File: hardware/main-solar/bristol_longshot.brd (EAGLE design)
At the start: 14 x 64 mm, 84 parts, among them U1 SAM_D20E, U10 TPS62243, U11 TPS3808, U12 74LVC1G04GW, U13 SPV1040, U14 LT4054ES5-4.2, U2 SI4060, U3 UBLOX_MAX, U4 TPS62243, U5 TG-5006CJ, U6 TG-5006CJ, U7 TPS3123, U8 SN74LVC1G32DCKR, U9 SE880, Y1 ABS05

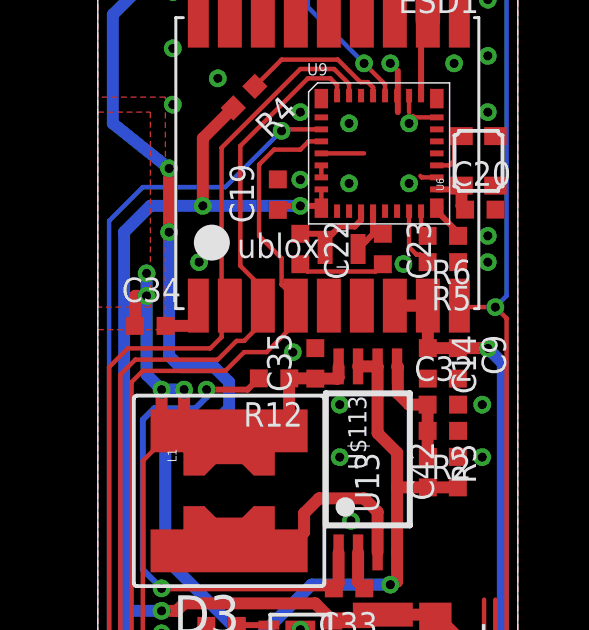
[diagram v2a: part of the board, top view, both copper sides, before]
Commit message: Added 0603 cap to vsolar
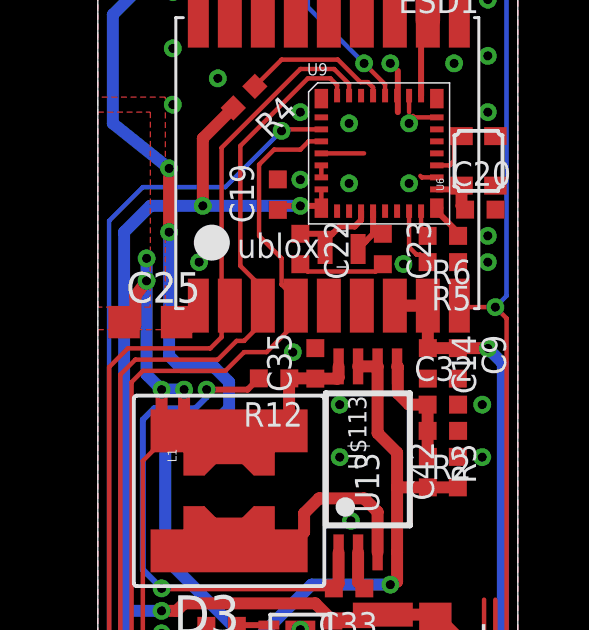
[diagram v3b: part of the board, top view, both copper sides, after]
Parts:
- removed C34: 4.7µF, microbuilder_v3:_0402
- added C25: 10µF, resistor:C0603K
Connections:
- net GND: now also C25.2; no longer C34.2
- net VSOLAR: now also C25.1; no longer C34.1
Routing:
- net GND: track 40.6 -> 39.6 mm
- net VSOLAR: track 52.6 -> 53.3 mm
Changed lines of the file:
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@@
 <element name="C33" library="microbuilder_v3" package="_0402" value="1nF" x="8.375" y="38.625" rot="R180"/>
 <element name="R12" library="microbuilder_v3" package="_0402" value="1kΩ" x="5.875" y="45.625" rot="R180"/>
-<element name="C34" library="microbuilder_v3" package="_0402" value="4.7µF" x="1.75" y="47.375"/>
 <element name="C35" library="microbuilder_v3" package="_0402" value="4.7µF" x="7.25" y="46.125" rot="R90"/>
 <element name="C36" library="microbuilder_v3" package="_0402" value="4.7µF" x="7" y="26.875"/>
@@
 <element name="R21" library="microbuilder_v3" package="_0402" value="DNP" x="5" y="26.875"/>
 <element name="L1" library="PecanFemto4" package="LPS3015" value="10uH LPS3015" x="4.375" y="41.875" rot="R270"/>
+<element name="C25" library="resistor" package="C0603K" value="10µF" x="1.75" y="47.5"/>
 </elements>
 <signals>
@@
 <contactref element="C31" pad="2"/>
 <contactref element="C33" pad="1"/>
-<contactref element="C34" pad="2"/>
 <contactref element="C35" pad="2"/>
 <contactref element="C36" pad="2"/>
@@
 <via x="7.5" y="25.125" extent="1-16" drill="0.3"/>
 <via x="12.8125" y="44.75" extent="1-16" drill="0.3"/>
-<wire x1="2.258" y1="47.375" x2="3.25" y2="47.375" width="0.4" layer="1"/>
 <via x="12.8125" y="43" extent="1-16" drill="0.3"/>
 <via x="8.0625" y="44.75" extent="1-16" drill="0.3"/>
@@
 <wire x1="1.5" y1="18.125" x2="1.383" y2="18.242" width="0.4" layer="1"/>
 <wire x1="1.383" y1="18.242" x2="1.375" y2="18.242" width="0.4" layer="1"/>
+<contactref element="C25" pad="2"/>
 </signal>
 <signal name="SWDIO">
@@
 <contactref element="U13" pad="8"/>
 <contactref element="C35" pad="1"/>
-<contactref element="C34" pad="1"/>
 <contactref element="U$113" pad="P$1"/>
 <wire x1="7.25" y1="45.617" x2="7.242" y2="45.625" width="0.4" layer="1"/>
@@
 <wire x1="6.25" y1="22.125" x2="1.75" y2="22.125" width="0.15" layer="1"/>
 <wire x1="1.75" y1="22.125" x2="1.5" y2="22.375" width="0.15" layer="1"/>
-<via x="1.625" y="49.125" extent="1-16" drill="0.3"/>
-<via x="1.625" y="48.375" extent="1-16" drill="0.3"/>
+<via x="1.625" y="49.625" extent="1-16" drill="0.3"/>
+<via x="1.625" y="48.875" extent="1-16" drill="0.3"/>
 <via x="2.125" y="45.25" extent="1-16" drill="0.3"/>
 <via x="2.875" y="45.25" extent="1-16" drill="0.3"/>
-<wire x1="1.625" y1="49.125" x2="1.625" y2="48.375" width="0.4" layer="16"/>
-<wire x1="1.625" y1="48.375" x2="1.625" y2="45.75" width="0.4" layer="16"/>
+<wire x1="1.625" y1="49.625" x2="1.625" y2="48.875" width="0.4" layer="16"/>
+<wire x1="1.625" y1="48.875" x2="1.625" y2="45.75" width="0.4" layer="16"/>
 <wire x1="1.625" y1="45.75" x2="2.125" y2="45.25" width="0.4" layer="16"/>
 <wire x1="2.125" y1="45.25" x2="2.875" y2="45.25" width="0.4" layer="16"/>
 <wire x1="2.125" y1="45.25" x2="2.125" y2="43.375" width="0.4" layer="1"/>
 <wire x1="2.875" y1="45.25" x2="2.875" y2="43.625" width="0.4" layer="1"/>
-<wire x1="1.242" y1="47.375" x2="1.25" y2="47.383" width="0.4" layer="1"/>
 <wire x1="1.25" y1="47.383" x2="1.25" y2="48.375" width="0.4" layer="1"/>
-<wire x1="1.25" y1="48.375" x2="1.625" y2="48.375" width="0.4" layer="1"/>
+<wire x1="1.25" y1="48.375" x2="1.625" y2="48.875" width="0.4" layer="1"/>
 <polygon width="0.2" layer="1">
 <vertex x="0" y="54.5"/>
@@
 <wire x1="3.32725" y1="42.5735" x2="3.361540625" y2="42.5735" width="0.2" layer="1"/>
 <wire x1="3.361540625" y1="42.5735" x2="3.552040625" y2="42.764" width="0.2" layer="1"/>
+<contactref element="C25" pad="1"/>
 </signal>
 <signal name="VBATT_SENSE">

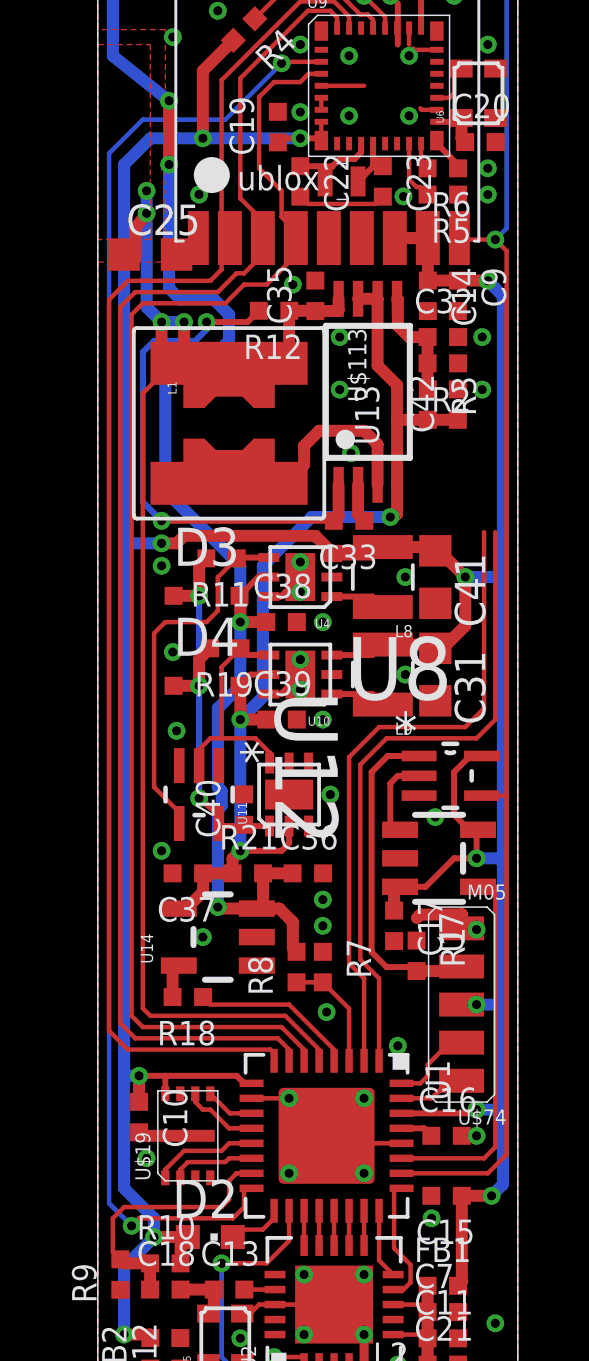
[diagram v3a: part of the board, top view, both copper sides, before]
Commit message: Updated many parts lists, updated bard numbering, removed makefiles for inactive things
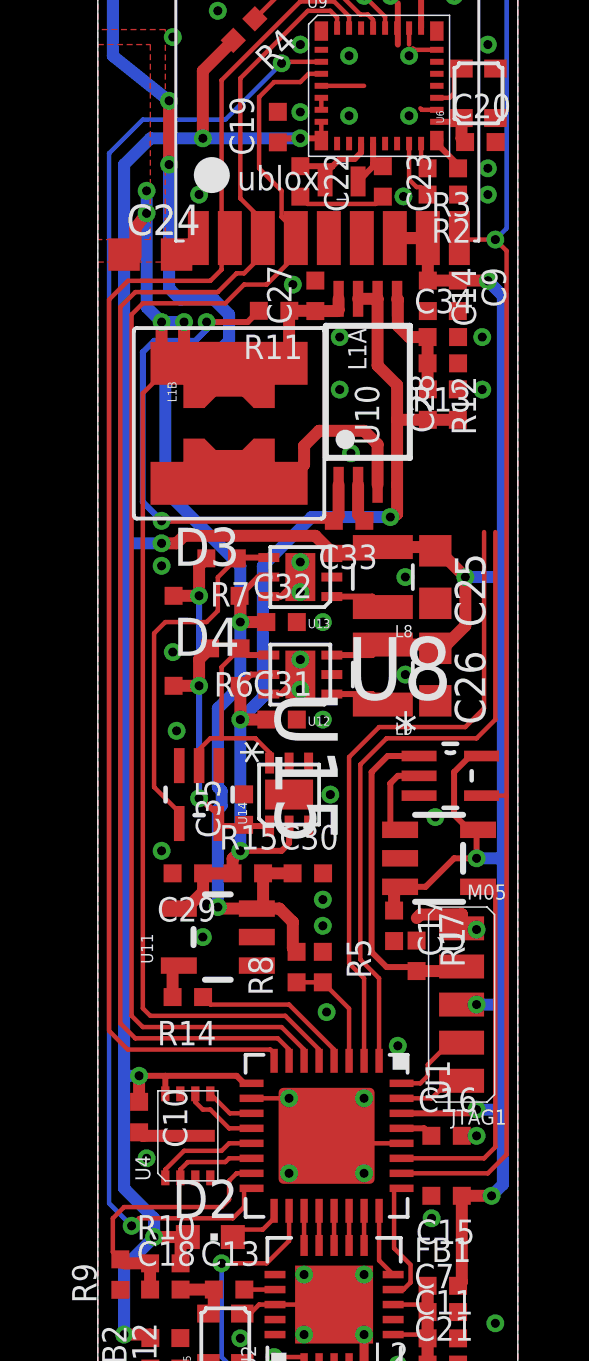
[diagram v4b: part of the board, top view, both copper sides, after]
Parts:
- removed C38, C39: 4.7µF, microbuilder_v3:_0402
- removed C40: 1nF, microbuilder_v3:_0402
- removed C41: 10µF, resistor:C0603K
- removed R19: 10kΩ, microbuilder_v3:_0402
- removed U$19: SST25WF040BT-40I/NP, fbri:USON-8
- added C24, C26: 10µF, resistor:C0603K
- added C27: 4.7µF, microbuilder_v3:_0402
- added C34: 1nF, microbuilder_v3:_0402
- added R13: 75kΩ/82kΩ, microbuilder_v3:_0402
- added U15: 74LVC1G04GW, 74LVC1G04GW_inverter:SOT65P210X110-5N
- C31: value 10µF -> 4.7µF; device resistor:C0603K -> microbuilder_v3:_0402
- C32: value 1nF -> 4.7µF
- C35: value 4.7µF -> 1nF
- R11: value 10kΩ -> 1kΩ
- R12: value 1kΩ -> 180kΩ/220kΩ
- R15: value DNP -> 0Ω/DNP
- R2: value 82kΩ -> 10kΩ
- R3: value 220kΩ -> 10kΩ
- U10: value TPS62243 -> SPV1040; device TPS62243:S-PWSON-N6 -> spv1040:TSSOP8
- U11: value TPS3808 -> LT4054ES5-4.2; device TPS3808:S-PWSON-N6 -> XYKlib:SOT23-5
- U12: value 74LVC1G04GW -> TPS62243; device 74LVC1G04GW_inverter:SOT65P210X110-5N -> TPS62243:S-PWSON-N6
- U13: value SPV1040 -> TPS62243; device spv1040:TSSOP8 -> TPS62243:S-PWSON-N6
- U14: value LT4054ES5-4.2 -> TPS3808; device XYKlib:SOT23-5 -> TPS3808:S-PWSON-N6
- U4: value TPS62243 -> SST25WF040BT-40I/NP; device TPS62243:S-PWSON-N6 -> fbri:USON-8
- moved R5 26.1 mm to (7.50, 23.8), turned to 270 degrees
- moved U4 19.0 mm to (3.00, 18.1), turned to 0 degrees
- moved R6 17.6 mm to (4.25, 34.4)
- moved C35 17.3 mm to (4.88, 29.0)
- moved C25 14.3 mm to (11.2, 36.8), turned to 270 degrees
- moved R7 14.0 mm to (4.12, 37.4), turned to 180 degrees
- moved C32 10.9 mm to (6.12, 35.2)
- moved R11 8.43 mm to (5.88, 45.6)
- moved R3 7.89 mm to (11.5, 50.4), turned to 180 degrees
- moved U10 7.34 mm to (8.50, 40.6)
- moved R12 6.00 mm to (11.0, 42.5), turned to 270 degrees
- moved R2 5.62 mm to (11.5, 49.5)
- moved C31 5.34 mm to (6.12, 32.0), turned to 0 degrees
- moved U11 5.31 mm to (4.00, 24.8), turned to 90 degrees
- moved U14 5.31 mm to (6.38, 29.5), turned to 0 degrees
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- renumbered C36 to C30, C37 to C29, C42 to C28, L1 to L1B, R18 to R14, R21 to R15, U$113 to L1A, U$74 to JTAG1
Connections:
- net 1.8V: now also C25.1, C26.1, U12.3, U13.3, U4.8; no longer C31.1, C41.1, U$19.8, U10.3, U4.3
- net BATTERY: now also C32.1, U11.3, U13.5; no longer C38.1, U14.3, U4.5
- net BATTERY_BUCK_SW: now also U13.1; no longer U4.1
- net BATTERY_EN: now also R7.1, U13.4, U15.4; no longer R11.1, U12.4, U4.4
- net CHG_STATUS: now also U11.1; no longer U14.1
- net CT: now also U14.3; no longer U11.3
- net GND: now also C24.2, C26.2, C27.2, C34.2, R13.1, R3.1, U11.2, U12.2, U12.6, U12.PAD, U13.6, U13.PAD, U14.5, U14.PAD, U15.3, U4.4, U4.P$9; no longer C38.2, C39.2, C40.2, C41.2, R6.1, R7.1, U$19.4, U$19.P$9, U10.6, U10.PAD, U11.5, U11.PAD, U12.3, U14.2, U4.2, U4.6, U4.PAD
- net LX1: now also U10.3; no longer U13.3
- net MEM_CSN: now also U4.1; no longer U$19.1
- net MEM_MISO: now also U4.2; no longer U$19.2
- net MEM_MOSI: now also U4.5; no longer U$19.5
- net MEM_SCK: now also U4.6; no longer U$19.6
- net MEM_WPN: now also U4.3; no longer U$19.3
- net MPP-SET: now also R11.2, U10.1; no longer R12.2, U13.1
- net MPPT-VOUT-TANK: now also C31.1, R12.2, U10.4, U10.6, U10.7, U11.4, U12.5, U14.2; no longer C39.1, R3.2, U10.5, U11.2, U13.4, U13.6, U13.7, U14.4
- net N$3: now also R3.2; no longer R6.2
- net N$5: now also R2.2; no longer R5.2
- net PROG: now also U11.5; no longer U14.5
- net SPV_VCTRL1: now also C34.1, R12.1, R13.2, U10.5; no longer C32.1, R2.2, R3.1, U13.5
- net SUPERVISOR_VCC: now also C35.1, R6.2, R7.2, U14.1, U15.5; no longer C40.1, R11.2, R19.2, U11.1, U12.5
- net TANK_BUCK_SW: now also U12.1; no longer U10.1
- net TANK_EN: now also R6.1, U12.4, U14.6, U15.2; no longer R19.1, U10.4, U11.6, U12.2
- net VBATT_SENSE: now also R5.2; no longer R7.2
- net VSOLAR: now also C24.1, C27.1, R11.1, U10.8; no longer C25.1, C35.1, R12.1, U13.8

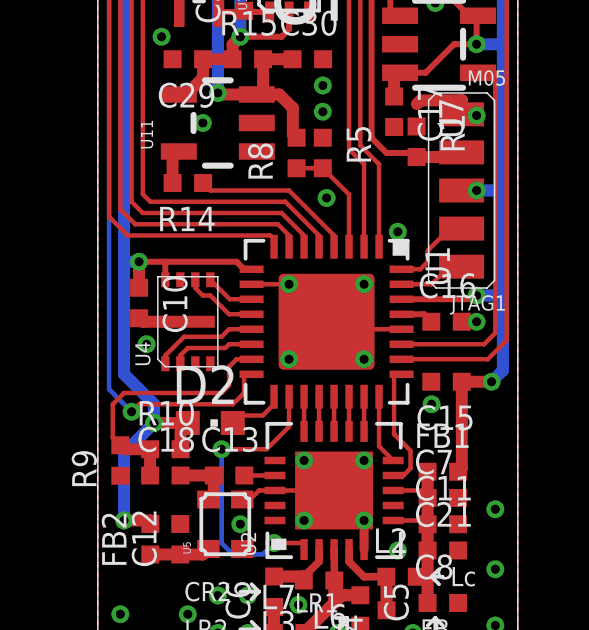
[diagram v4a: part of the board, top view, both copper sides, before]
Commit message: [Bugfix] Memory HOLD pin needs to be high. Also adjusted pad/cream size. Bump to V0.98x.1
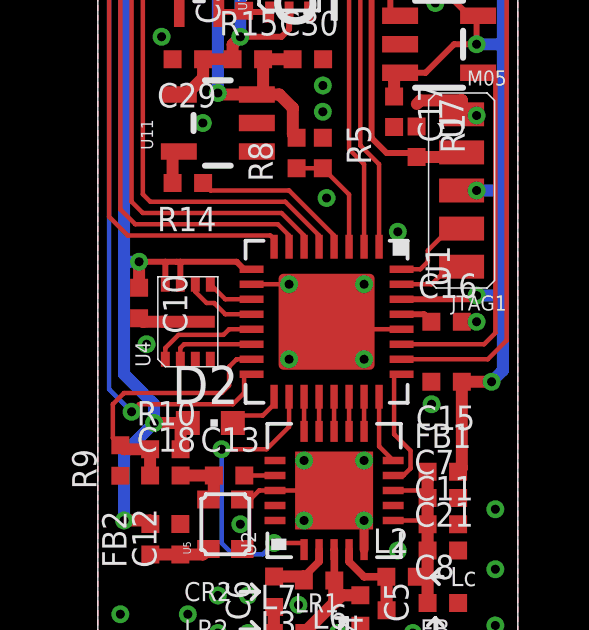
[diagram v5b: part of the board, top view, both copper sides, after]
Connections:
- net 1.8V: now also U4.7
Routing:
- net 1.8V: track 136.6 -> 137.5 mm
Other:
- board text added: "V0.981.1"
- board text removed: "V0.981.0"
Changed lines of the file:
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@@
 <setting verticaltext="up"/>
 </settings>
-<grid distance="1" unitdist="mm" unit="mm" style="lines" multiple="1" display="yes" altdistance="0.025" altunitdist="inch" altunit="inch"/>
+<grid distance="0.125" unitdist="mm" unit="mm" style="lines" multiple="1" display="yes" altdistance="0.025" altunitdist="inch" altunit="inch"/>
 <layers>
 <layer number="1" name="Top" color="4" fill="1" visible="yes" active="yes"/>
@@
 <wire x1="1.625" y1="62.875" x2="0.625" y2="63.375" width="0.2" layer="29" curve="-75"/>
 <wire x1="1.625" y1="55.875" x2="0.625" y2="55.375" width="0.2" layer="29"/>
-<text x="2.25" y="59.75" size="0.8" layer="29" font="vector" ratio="14">V0.981.0</text>
+<text x="2.25" y="59.75" size="0.8" layer="29" font="vector" ratio="14">V0.981.1</text>
 <rectangle x1="0.25" y1="48" x2="1.75" y2="54.5" layer="29"/>
 <rectangle x1="9" y1="59.25" x2="12" y2="63.25" layer="30"/>
@@
 <contactref element="U4" pad="8"/>
 <wire x1="1.375" y1="20.125" x2="2.25" y2="20.125" width="0.2" layer="1"/>
-<wire x1="2.25" y1="20.125" x2="4.625" y2="20.125" width="0.2" layer="1"/>
+<wire x1="2.25" y1="20.125" x2="2.625" y2="20.125" width="0.2" layer="1"/>
+<wire x1="2.75" y1="20.125" x2="4.625" y2="20.125" width="0.2" layer="1"/>
 <wire x1="4.625" y1="20.125" x2="4.875" y2="19.875" width="0.2" layer="1"/>
 <wire x1="4.875" y1="19.875" x2="5.125" y2="19.875" width="0.2" layer="1"/>
-<wire x1="2.25" y1="19.525" x2="2.25" y2="20.125" width="0.2" layer="1"/>
+<wire x1="2.25" y1="19.375" x2="2.25" y2="20.125" width="0.2" layer="1"/>
 <wire x1="1.375" y1="19.258" x2="1.375" y2="20.125" width="0.4" layer="1"/>
 <wire x1="3.5" y1="53.625" x2="4.5157875" y2="54.6407875" width="0.4" layer="1"/>
@@
 <wire x1="2.125" y1="37.875" x2="0.875" y2="37.875" width="0.4" layer="16"/>
 <wire x1="7.8" y1="37.55" x2="7.8" y2="37.575" width="0.4" layer="1"/>
+<contactref element="U4" pad="7"/>
+<wire x1="2.75" y1="19.375" x2="2.75" y2="20.125" width="0.2" layer="1"/>
+<wire x1="2.75" y1="20.125" x2="2.625" y2="20.125" width="0.2" layer="1"/>
 </signal>
 <signal name="VDD_CORE">
@@
 <contactref element="U4" pad="5"/>
 <contactref element="U1" pad="11"/>
-<wire x1="5.125" y1="18.875" x2="4.4" y2="18.875" width="0.15" layer="1"/>
-<wire x1="4.4" y1="18.875" x2="3.75" y2="19.525" width="0.15" layer="1"/>
+<wire x1="5.125" y1="18.875" x2="4.25" y2="18.875" width="0.15" layer="1"/>
+<wire x1="4.25" y1="18.875" x2="3.75" y2="19.375" width="0.15" layer="1"/>
 </signal>
 <signal name="MEM_CSN">
@@
 <contactref element="U1" pad="13"/>
 <wire x1="5.125" y1="17.875" x2="4.375" y2="17.875" width="0.15" layer="1"/>
-<wire x1="4.375" y1="17.875" x2="4.125" y2="17.625" width="0.15" layer="1"/>
-<wire x1="4.125" y1="17.625" x2="2.875" y2="17.625" width="0.15" layer="1"/>
-<wire x1="2.875" y1="17.625" x2="2.25" y2="17" width="0.15" layer="1"/>
-<wire x1="2.25" y1="17" x2="2.25" y2="16.725" width="0.15" layer="1"/>
+<wire x1="4.375" y1="17.875" x2="4.1875" y2="17.6875" width="0.15" layer="1"/>
+<wire x1="4.1875" y1="17.6875" x2="2.6875" y2="17.6875" width="0.15" layer="1"/>
+<wire x1="2.25" y1="17" x2="2.25" y2="16.875" width="0.15" layer="1"/>
+<wire x1="2.6875" y1="17.6875" x2="2.25" y2="17.25" width="0.15" layer="1"/>
+<wire x1="2.25" y1="17.25" x2="2.25" y2="16.875" width="0.15" layer="1"/>
 </signal>
 <signal name="GIMO">
@@
 <contactref element="U4" pad="6"/>
 <contactref element="U1" pad="12"/>
-<wire x1="5.125" y1="18.375" x2="4.375" y2="18.375" width="0.15" layer="1"/>
-<wire x1="4.375" y1="18.375" x2="3.75" y2="19" width="0.15" layer="1"/>
-<wire x1="3.75" y1="19" x2="3.5" y2="19" width="0.15" layer="1"/>
-<wire x1="3.5" y1="19" x2="3.25" y2="19.25" width="0.15" layer="1"/>
-<wire x1="3.25" y1="19.25" x2="3.25" y2="19.525" width="0.15" layer="1"/>
+<wire x1="5.125" y1="18.375" x2="4.25" y2="18.375" width="0.15" layer="1"/>
+<wire x1="4.25" y1="18.375" x2="3.875" y2="18.75" width="0.15" layer="1"/>
+<wire x1="3.875" y1="18.75" x2="3.625" y2="18.75" width="0.15" layer="1"/>
+<wire x1="3.625" y1="18.75" x2="3.25" y2="19.125" width="0.15" layer="1"/>
+<wire x1="3.25" y1="19.125" x2="3.25" y2="19.375" width="0.15" layer="1"/>
 </signal>
 <signal name="MEM_MISO">
 <contactref element="U4" pad="2"/>
 <contactref element="U1" pad="14"/>
-<wire x1="5.125" y1="17.375" x2="4.375" y2="17.375" width="0.15" layer="1"/>
-<wire x1="4.375" y1="17.375" x2="4.25" y2="17.25" width="0.15" layer="1"/>
-<wire x1="4.25" y1="17.25" x2="3" y2="17.25" width="0.15" layer="1"/>
-<wire x1="3" y1="17.25" x2="2.75" y2="17" width="0.15" layer="1"/>
-<wire x1="2.75" y1="17" x2="2.75" y2="16.725" width="0.15" layer="1"/>
+<wire x1="5.125" y1="17.375" x2="2.875" y2="17.375" width="0.15" layer="1"/>
+<wire x1="2.75" y1="17" x2="2.75" y2="16.875" width="0.15" layer="1"/>
+<wire x1="2.875" y1="17.375" x2="2.75" y2="17.25" width="0.15" layer="1"/>
+<wire x1="2.75" y1="17.25" x2="2.75" y2="16.875" width="0.15" layer="1"/>
 </signal>
 <signal name="SI_MOSI">

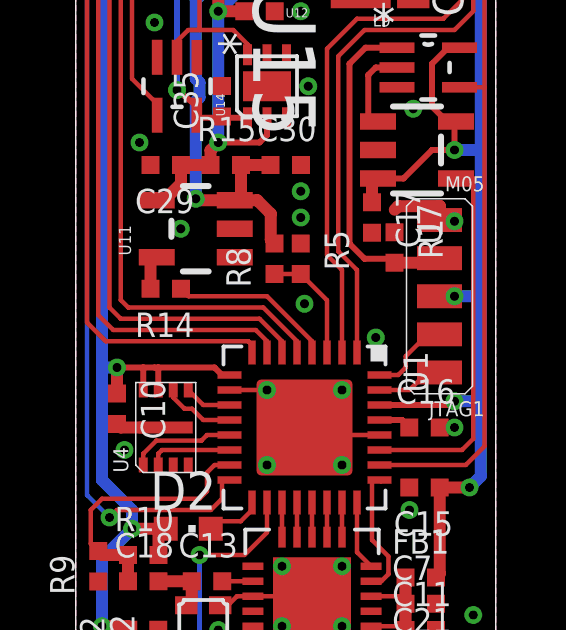
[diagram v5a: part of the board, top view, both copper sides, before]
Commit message: Added vias though all the pads on the debug connector
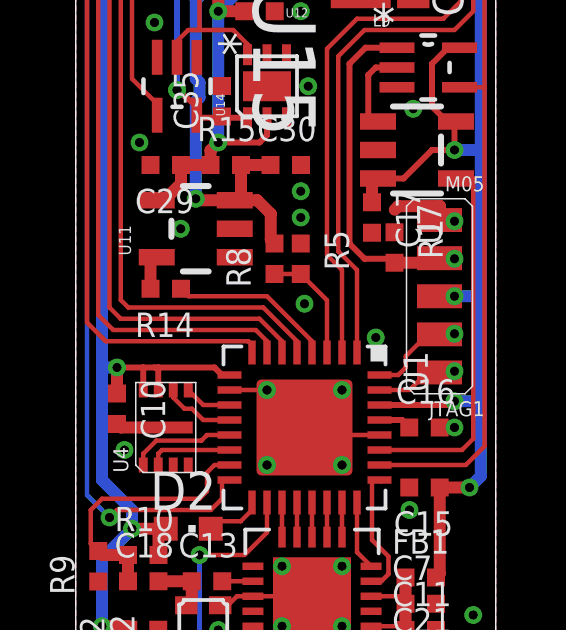
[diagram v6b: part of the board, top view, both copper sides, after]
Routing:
- net SWDCLK: track 2.24 -> 2.78 mm, vias 0 -> 1
- net SWDIO: track 2.78 -> 3.30 mm, vias 0 -> 1
- net EXT!RESET: track 11.1 -> 11.7 mm, vias 0 -> 1
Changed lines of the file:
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@@
 <wire x1="11.625" y1="21.125" x2="12.02" y2="21.125" width="0.15" layer="1"/>
 <wire x1="12.02" y1="21.125" x2="12.125" y2="21.23" width="0.15" layer="1"/>
+<via x="12.625" y="21.25" extent="1-16" drill="0.3"/>
+<wire x1="12.625" y1="21.25" x2="12.125" y2="21.25" width="0.2" layer="1"/>
+<wire x1="12.125" y1="21.25" x2="12.125" y2="21.23" width="0.2" layer="1"/>
 </signal>
 <signal name="SWDCLK">
@@
 <wire x1="11.5" y1="19.75" x2="11.915" y2="19.75" width="0.15" layer="1"/>
 <wire x1="11.915" y1="19.75" x2="12.125" y2="19.96" width="0.15" layer="1"/>
+<via x="12.625" y="20" extent="1-16" drill="0.3"/>
+<wire x1="12.125" y1="19.96" x2="12.625" y2="19.96" width="0.2" layer="1"/>
+<wire x1="12.625" y1="19.96" x2="12.625" y2="20" width="0.2" layer="1"/>
 </signal>
 <signal name="KEY">
@@
 <wire x1="9.625" y1="23.75" x2="10.492" y2="23.75" width="0.2" layer="1"/>
 <wire x1="10.492" y1="23.75" x2="10.625" y2="23.617" width="0.2" layer="1"/>
+<via x="12.625" y="23.75" extent="1-16" drill="0.3"/>
+<wire x1="12.625" y1="23.75" x2="12.125" y2="23.75" width="0.2" layer="1"/>
+<wire x1="12.125" y1="23.75" x2="12.125" y2="23.77" width="0.2" layer="1"/>
 </signal>
 <signal name="SAM_XOSC">
